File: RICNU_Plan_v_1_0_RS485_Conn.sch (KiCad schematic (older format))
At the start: 2 parts, among them J4 DF52-4S-0.8H(21)

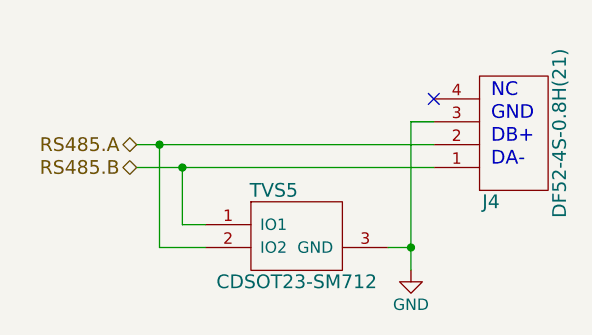
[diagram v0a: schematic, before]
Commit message: Re-routed CAN, RS-485, and debug connectors (wrong polarity in all)
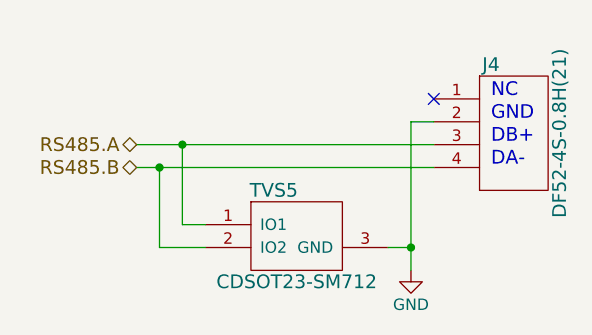
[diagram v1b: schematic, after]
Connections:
- net GND: now also J4.2; no longer J4.3
- net RS485.A: now also J4.3, TVS5.1 (IO1); no longer J4.2, TVS5.2 (IO2)
- net RS485.B: now also J4.4, TVS5.2 (IO2); no longer J4.1, TVS5.1 (IO1)
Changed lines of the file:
@@
 F 3 "" H 6750 3750 60  0001 C CNN
 	1    6750 3750
-	1    0    0    1
+	1    0    0    -1
 $EndComp
 Text Notes 6650 3600 0    60   ~ 0
@@
 Wire Wire Line
 	5400 4150 5300 4150
-Wire Wire Line
-	5300 4150 5300 3900
-Connection ~ 5300 3900
+Connection ~ 5200 3900
 Wire Wire Line
 	5400 4250 5200 4250
-Wire Wire Line
-	5200 4250 5200 3800
-Connection ~ 5200 3800
+Connection ~ 5300 3800
 $Comp
-L GND #PWR065
+L GND #PWR066
 U 1 1 59FAEED6
 P 6300 4350
-F 0 "#PWR065" H 6300 4100 50  0001 C CNN
+F 0 "#PWR066" H 6300 4100 50  0001 C CNN
 F 1 "GND" H 6300 4200 50  0000 C CNN
 F 2 "" H 6300 4350 50  0001 C CNN
@@
 Text Notes 6650 3900 0    60   ~ 0
 DA-
+Wire Wire Line
+	5300 4150 5300 3800
+Wire Wire Line
+	5200 4250 5200 3900
 $EndSCHEMATC
